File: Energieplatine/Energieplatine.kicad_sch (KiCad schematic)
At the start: 39 parts, among them J2 Conn_01x02_Pin, J3 Conn_01x02_Pin, J4 Conn_02x07_Odd_Even, J5 Conn_01x02_Pin, J6 Conn_01x02_Pin, J7 USB3_A, Q1 IRF9540N, Q2 IRF9540N, Q3 IRF540N, U1 4027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

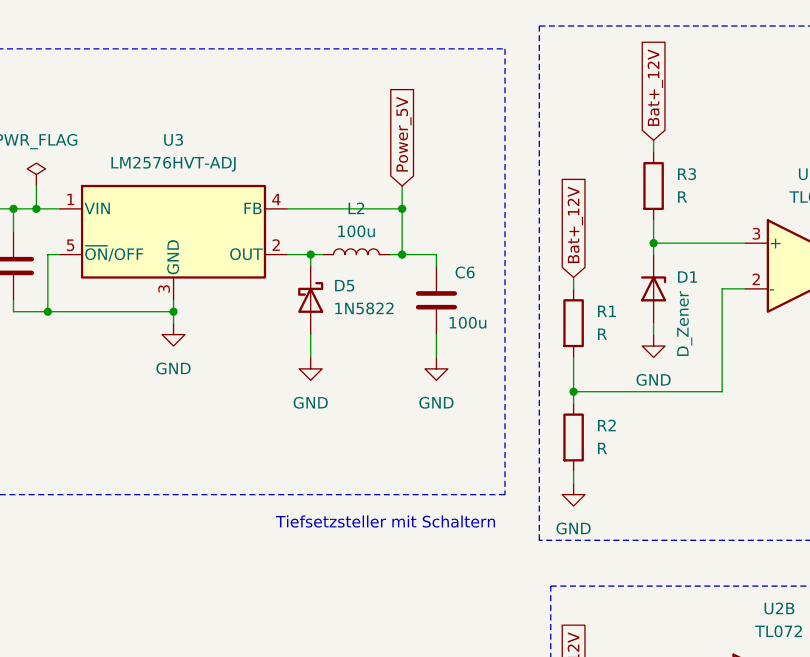
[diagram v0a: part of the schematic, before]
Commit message: Feedbackloop vom TSS hinzugefügt
Spannungsteiler am Ende des TSS für die Feedbackloop hinzugefügt
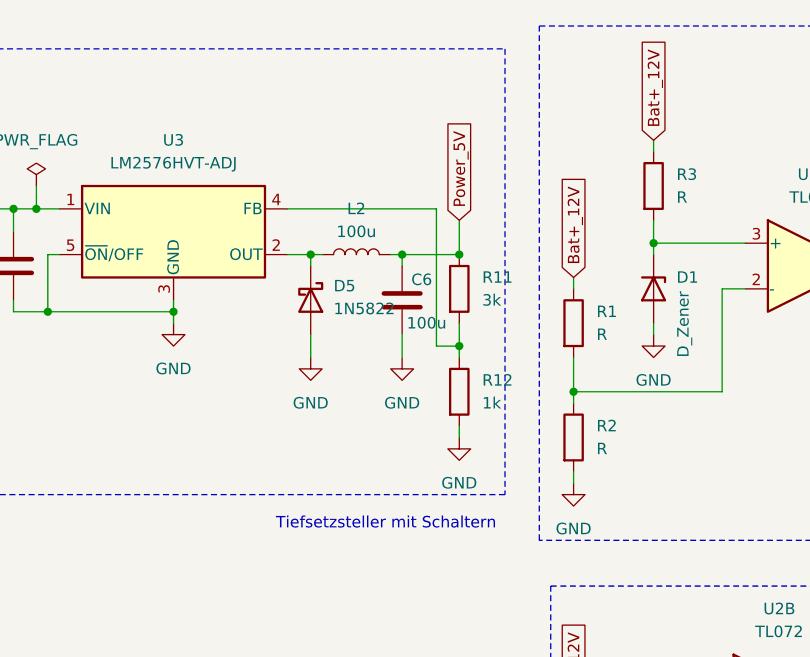
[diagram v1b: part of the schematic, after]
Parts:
- added R11: 3k, symbol Device:R
- added R12: 1k, symbol Device:R
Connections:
- net GND: now also R12.2
- net Power_5V: now also R11.1; no longer U3.4 (FB)
- new net: R11.2, R12.1, U3.4 (FB)
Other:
- moved on the sheet: C6

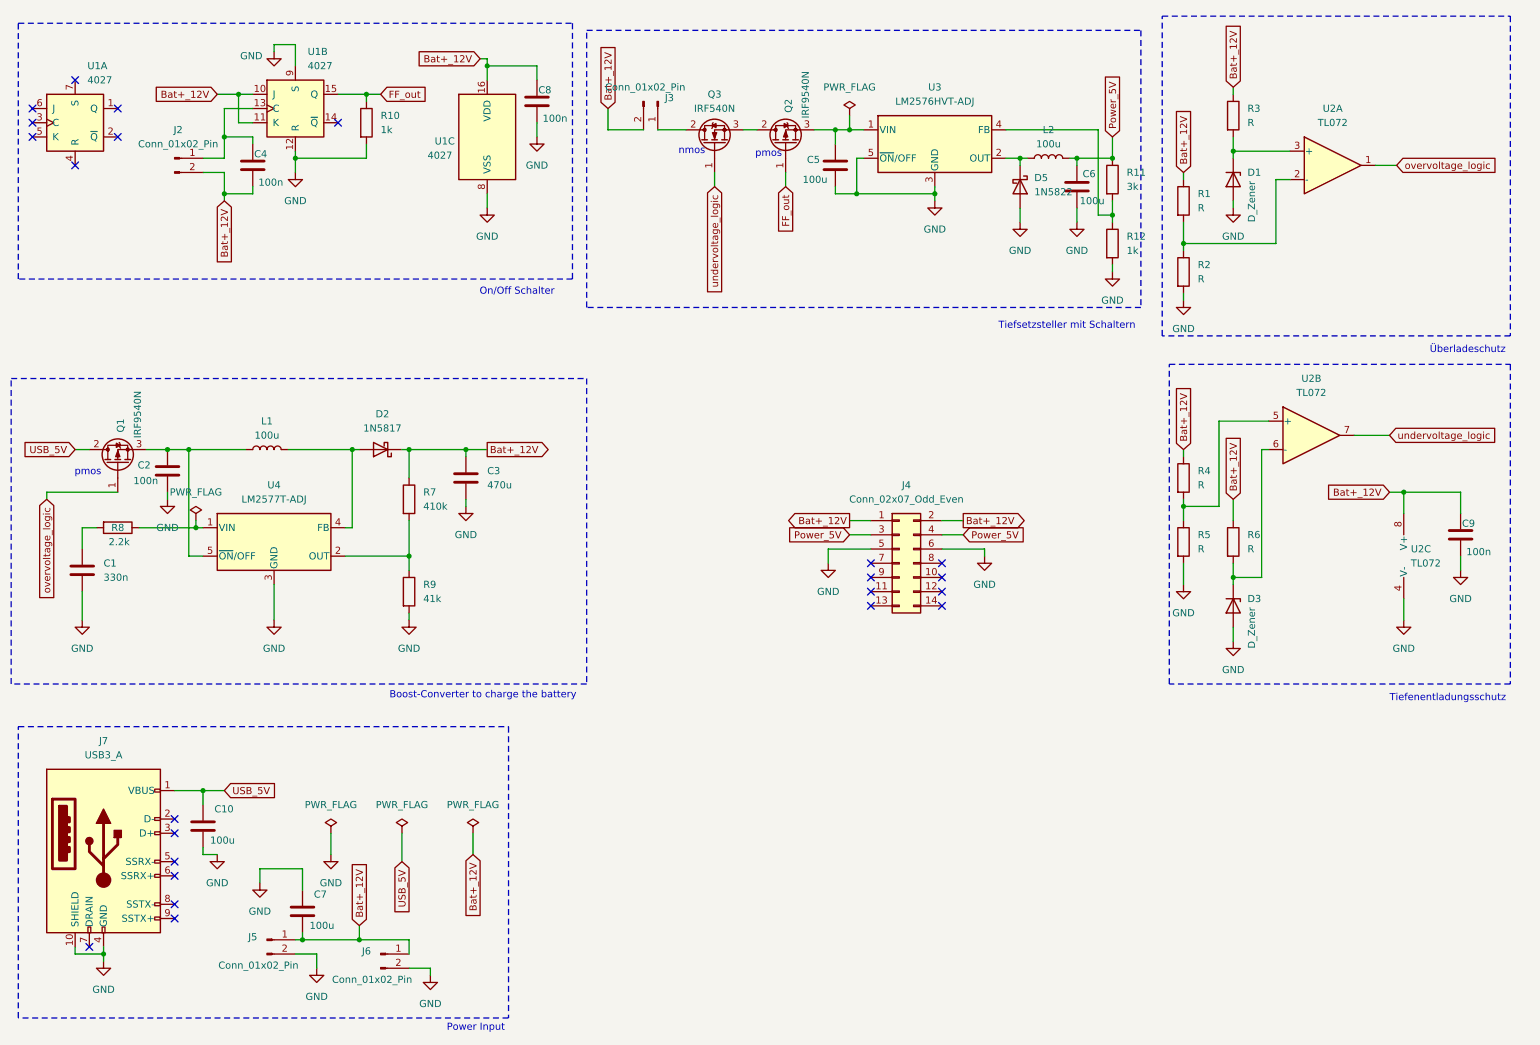
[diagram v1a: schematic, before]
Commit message: Platine Verbessert und Fehler gefixed
kein Layout geupdated
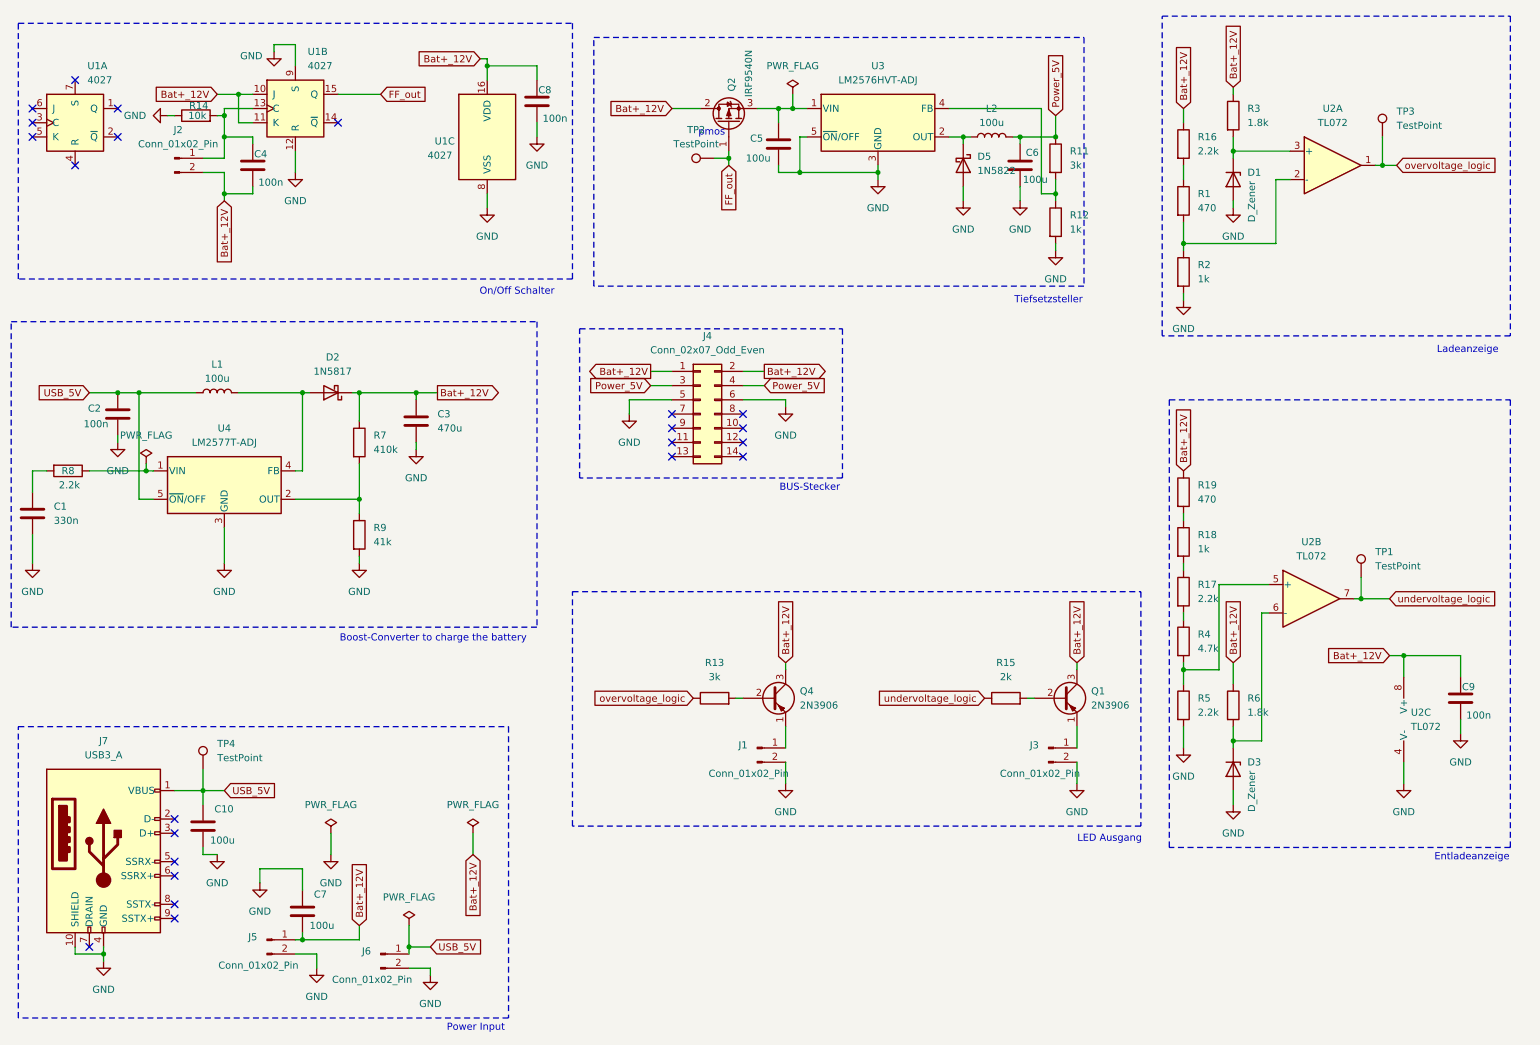
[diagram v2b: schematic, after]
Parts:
- removed Q1: IRF9540N, Package_TO_SOT_THT:TO-220-3_Vertical, symbol Transistor_FET:IRF9540N
- removed Q3: IRF540N, Package_TO_SOT_THT:TO-220-3_Vertical, symbol Transistor_FET:IRF540N
- removed R10: 1k, Resistor_THT:R_Axial_DIN0207_L6.3mm_D2.5mm_P7.62mm_Horizontal, symbol Device:R
- added J1: Conn_01x02_Pin, Connector_PinHeader_2.00mm:PinHeader_1x02_P2.00mm_Vertical, symbol Connector:Conn_01x02_Pin
- added Q1, Q4: 2N3906, Package_TO_SOT_THT:TO-92_Inline, symbol Transistor_BJT:2N3906
- added R13: 3k, Resistor_THT:R_Axial_DIN0207_L6.3mm_D2.5mm_P7.62mm_Horizontal, symbol Device:R
- added R14: 10k, Resistor_THT:R_Axial_DIN0207_L6.3mm_D2.5mm_P7.62mm_Horizontal, symbol Device:R
- added R15: 2k, Resistor_THT:R_Axial_DIN0207_L6.3mm_D2.5mm_P7.62mm_Horizontal, symbol Device:R
- added R16, R17: 2.2k, Resistor_THT:R_Axial_DIN0207_L6.3mm_D2.5mm_P7.62mm_Horizontal, symbol Device:R
- added R18: 1k, Resistor_THT:R_Axial_DIN0207_L6.3mm_D2.5mm_P7.62mm_Horizontal, symbol Device:R
- added R19: 470, Resistor_THT:R_Axial_DIN0207_L6.3mm_D2.5mm_P7.62mm_Horizontal, symbol Device:R
- added TP1, TP2, TP3, TP4: TestPoint, Connector_Pin:Pin_D0.7mm_L6.5mm_W1.8mm_FlatFork, symbol Connector:TestPoint
- R1: value R -> 470
- R2: value R -> 1k
- R3, R6: value R -> 1.8k
- R4: value R -> 4.7k
- R5: value R -> 2.2k
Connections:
- net Bat+_12V: now also Q2.2 (D), Q1.3 (C), Q4.3 (C), R16.1, R19.1; no longer J3.2 (Pin_2), J6.1 (Pin_1), R1.1, R4.1
- net FF_out: now also TP2.1
- net GND: now also J3.2 (Pin_2), J1.2 (Pin_2), R14.1
- net USB_5V: now also C2.1, J6.1 (Pin_1), L1.1, U4.5 (~{ON}/OFF), TP4.1
- net overvoltage_logic: now also R13.1, TP3.1
- net undervoltage_logic: now also R15.1, TP1.1
- net at J3.1 (Pin_1): now also Q1.1 (E)
- net at C4.1, J2.1 (Pin_1), U1.13 (C): now also R14.2
- new net: R18.1, R19.2
- new net: R17.1, R18.2
- new net: R1.1, R16.2
- new net: J1.1 (Pin_1), Q4.1 (E)
- new net: Q4.2 (B), R13.2
- new net: Q1.2 (B), R15.2
- new net: R17.2, R4.1
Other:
- note added: "BUS-Stecker"
- note added: "Entladeanzeige"
- note added: "LED Ausgang"
- note added: "Ladeanzeige"
- note added: "Tiefsetzsteller"
- note removed: "Tiefenentladungsschutz"
- note removed: "Tiefsetzsteller mit Schaltern"
- note removed: "nmos"
- note removed: "Überladeschutz"
- moved on the sheet: C1, C2, C3, C5, C6, C9, D2, D3, D5, J4, L1, L2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
